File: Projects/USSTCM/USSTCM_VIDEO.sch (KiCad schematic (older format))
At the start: 11 parts

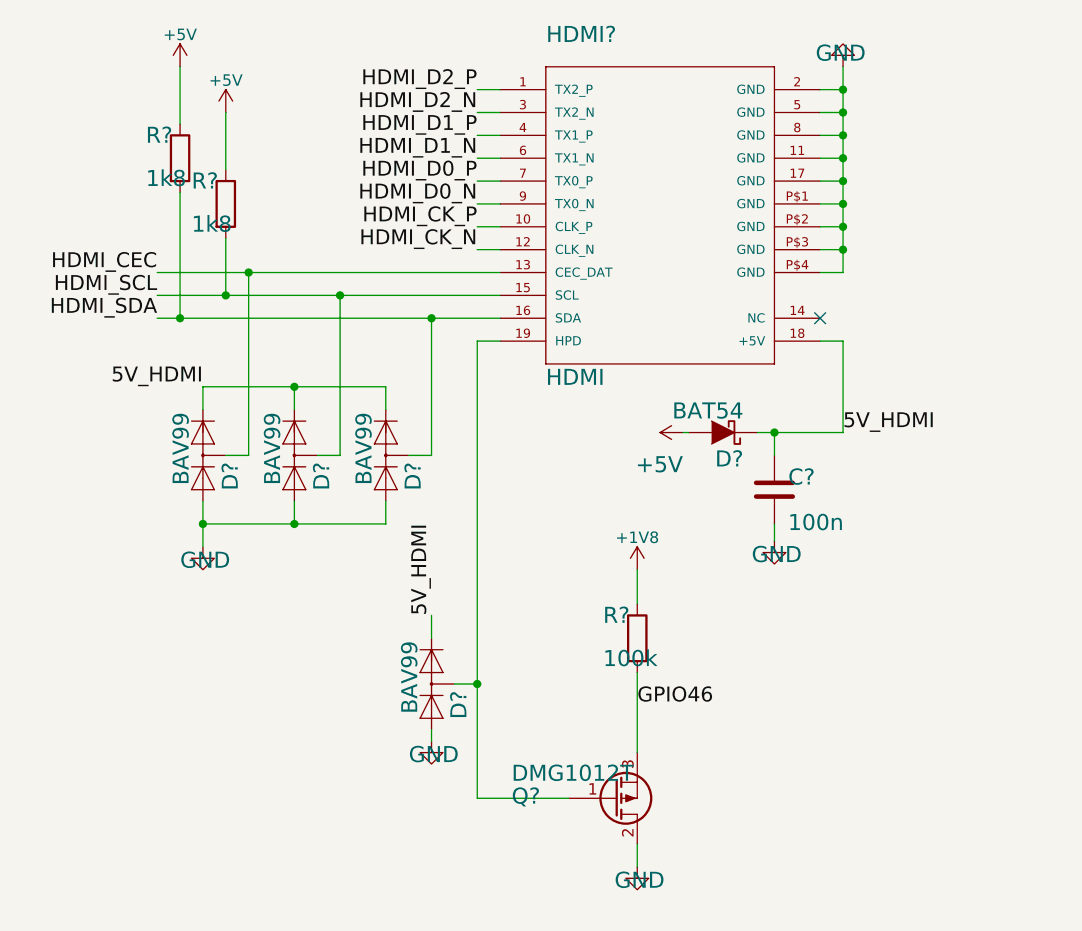
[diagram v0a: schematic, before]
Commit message: added differential routes
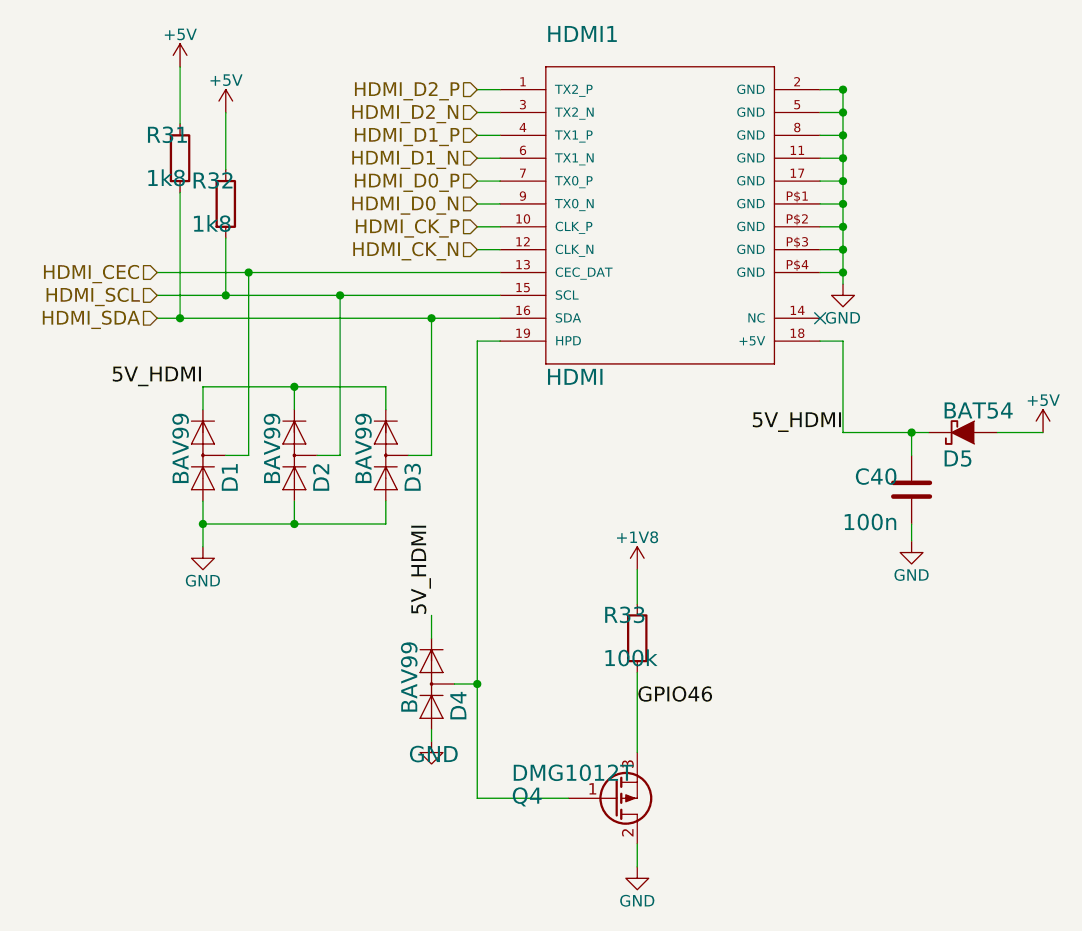
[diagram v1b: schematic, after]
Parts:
- C40: renamed from C?; footprint USSTCM:RCL_C0603 -> Capacitors_SMD:C_0805
- R31, R32, R33: renamed from R?; footprint USSTCM:RCL_R0603 -> Resistors_SMD:R_0805
- gave numbers to parts that had none: 7
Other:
- moved on the sheet: C40, D5
